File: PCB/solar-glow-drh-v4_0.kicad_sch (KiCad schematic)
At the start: 66 parts, among them J1 UPDI hdr, Q2 BSS138LT1G, SW2 LED master, U1 AVR64EA28 (VQFN28), U3 ADXL367, U5 NT3H2211, U6 TPS22917, U7 MB85RC512TY, U8 AEM10300, U9 TPS7A0233 (SOT23-5*)

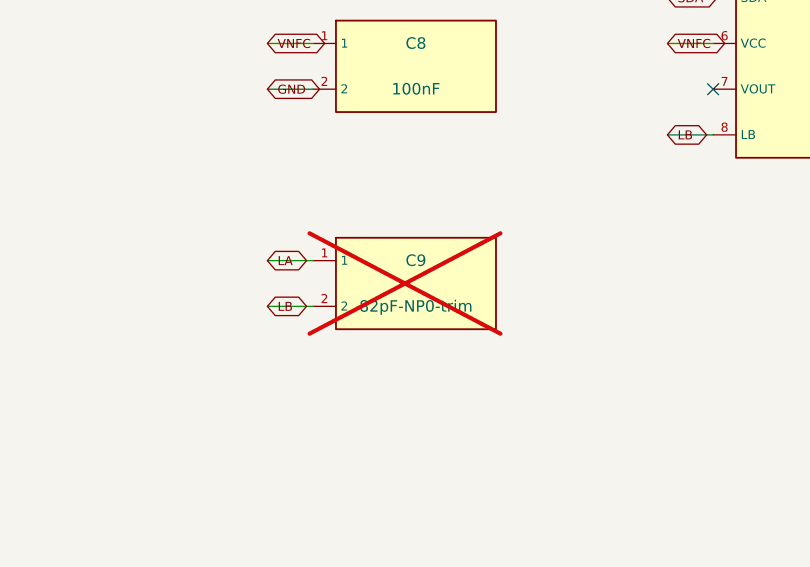
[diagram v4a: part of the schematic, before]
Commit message: C9: 82 pF DNP -> 47 pF placed, from a derivation rather than a bench trim
C9 was a hand-fitted trim. It is now a reflowed 47 pF part, because the value
can be computed and the computation lands well inside the window the trim would
have searched.

THE COIL. No closed form fits it: Wheeler, Mohan and Jenei are all fitted to
square spirals and this coil is 11.0 x 24.6 mm outer, aspect 2.2. So it is
Greenhouse on the board's own rails -- 7 turns read straight out of the .kicad_pcb
at x 37.4-41.0 / 44.8-48.4 and y 32.2-35.8 / 53.2-56.8, 0.30 mm trace on 0.60 mm
pitch -- summing the self-inductance of all 28 segments and the signed mutual
inductance of every parallel pair, GMD-corrected for strip width, 45-degree
corners taken off first order.

    L = 0.958 uH bare.  404 nH self + 606 nH mutual: 60% of this coil is coupling.

Checked twice. The same code agrees with Mohan's current-sheet fit to 2-6% on
square spirals, where that fit is valid. And PCB-side-notes §5's existing "~90 pF
bare" figure implies L = 0.957 uH at 13.56 MHz -- the same coil to three digits,
reached by whoever wrote that line without this calculation.

THE REST. Ci = 50 pF (NT3H2211 Table 42, LA-LB on-chip, 2.4 Vrms, 44/56 limits).
Cc = 6 pF (AN11276 Table 2: etched inter-turn 2-4, bridge 1-5 -- this coil's inner
end does return across the front on LB, which is that bridge).

THE TARGET IS NOT 13.56. AN11276 4.2.1: "For single tag operation, a tuning
slightly above 13.56 MHz would lead to maximum read-/write distance. Due to
manufacturing tolerances, a nominal frequency of 14.5 MHz for single tag operation
is recommended." Presenting the card couples the antennas and pulls the tag DOWN,
so a tag under the carrier gets worse as it approaches and one above it improves.

THE FERRITE IS A SCENARIO, NOT A TOLERANCE. §5's old 52-77 pF enclosed window is
an inductance window in disguise: +10% to +36%. Every board shares whichever
multiplier is real, so it is spanned, not stacked in quadrature with the comp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
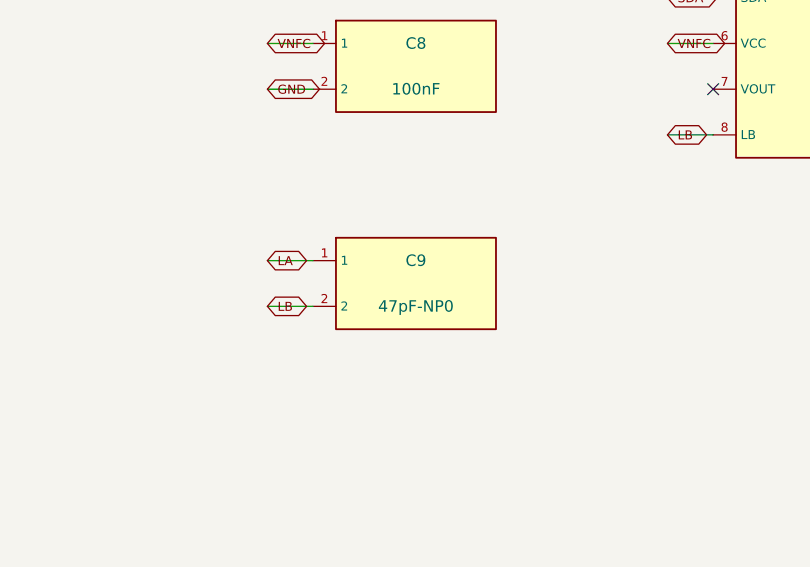
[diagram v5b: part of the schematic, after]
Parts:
- C9: value 82pF-NP0-trim -> 47pF-NP0; MPN QSCT251Q820G1GV001E -> QSCT251Q470G1GV001E; Supplier P/N 712-QSCT251Q820G1GV001ETR-ND -> 712-QSCT251Q470G1GV001ETR-ND; now fitted
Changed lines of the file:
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@@
 		(on_board yes)
 		(in_pos_files yes)
-		(dnp yes)
+		(dnp no)
 		(property "Reference" "C9"
 			(at 571.5 119.38 0)
@@
 			)
 		)
-		(property "Value" "82pF-NP0-trim"
+		(property "Value" "47pF-NP0"
 			(at 571.5 124.46 0)
 			(show_name no)
@@
 			)
 		)
-		(property "Description" "NFC tank trim, 0805 high-Q C0G +/-2% (Johanson S-series). DNP at assembly - hand-fit on the bench to land resonance at 13.56 MHz; U5 carries ~50 pF internally. Value is a STARTING POINT, trim 68-100 pF."
+		(property "Description" "NFC tank trim, 0805 high-Q C0G +/-2% (Johanson S-series, ultra-low ESR). PLACED at assembly as of 2026-07-30 - value derived, not trimmed: coil L = 0.958 uH by Greenhouse on the board's 7 rails, ferrite-loaded 1.05-1.30 uH, tag Ci = 50 pF (NT3H2211 Table 42), antenna Cc = 6 pF (AN11276 Table 2). 47 pF lands the enclosed resonance at 14.45 MHz against AN11276 4.2.1's 14.5 MHz single-tag target and stays above the 13.56 carrier across the whole ferrite range. Was 82 pF + DNP, which sat at 12.5 MHz enclosed - under the carrier, the wrong side to miss on."
 			(at 560.07 119.38 0)
 			(hide yes)
@@
 			)
 		)
-		(property "MPN" "QSCT251Q820G1GV001E"
+		(property "MPN" "QSCT251Q470G1GV001E"
 			(at 560.07 119.38 0)
 			(hide yes)
@@
 			)
 		)
-		(property "Supplier P/N" "712-QSCT251Q820G1GV001ETR-ND"
+		(property "Supplier P/N" "712-QSCT251Q470G1GV001ETR-ND"
 			(at 560.07 119.38 0)
 			(hide yes)

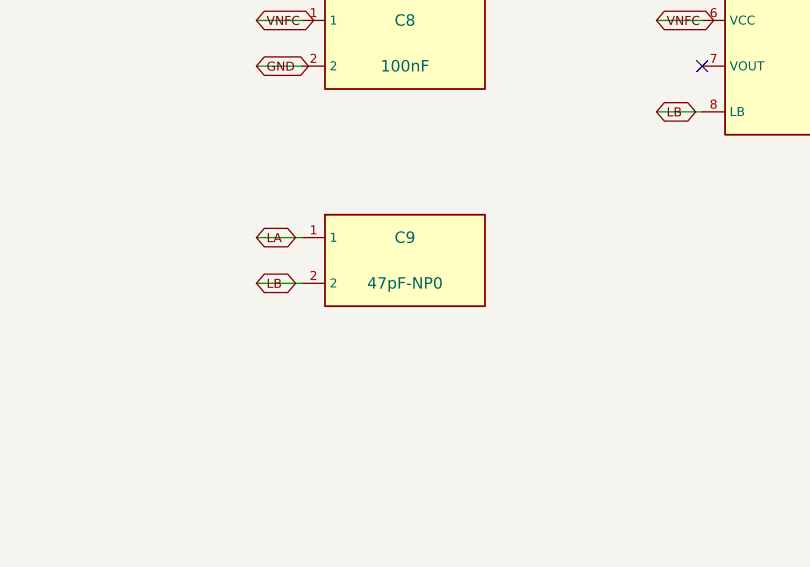
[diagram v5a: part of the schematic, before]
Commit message: Second full passive audit: two re-picks needed, one corner-case, C9 value fix
All 35 passives, audited holistically: schematic + board + BOM cross-check,
per-pad nets, node worst-case voltages, DC-bias derating, datasheet-required
values for every IC's externals, and a live two-distributor sourcing sweep.

FINDING 1 (the real one). C25, the AEM10300's CSRC/BUFSRC buffer, is
GRT188R61A226ME13D -- 0603, 22 uF, X5R, 10 V. The AEM's table says CSRC min 13 /
typ 22 uF, and its footnote says verbatim: "Consider all component tolerance and
deratings. Typically, DC-bias derating has a major impact on capacitance on
ceramic capacitors." BUFSRC rides the MPP at 3.1-3.5 V and touches VOC 4.15 V; a
0603 22 uF/10 V X5R loses 45-60% there, leaving ~9-12 uF -- under the minimum
the footnote exists to warn about. Fix verified in stock and verified to FIT:
TDK C2012X5R1C226M125AC (0805, 16 V, 1.25 mm, 11,799 at DK) gives ~15-17 uF
effective; measured neighbour gaps at C25 (SC3 0.529 / L2 0.575 / SB2 0.776 mm)
leave >=0.28 mm after 0603->0805 growth. A 1206 does not fit (L2 would be at
0.02 mm). part_heights "C25": 0.90 -> 1.25 with the swap.

FINDING 2. C26/C27's GRM21BR71A106KA73L (0805 10 uF X7R 10 V): zero stock at
DigiKey in all three package types AND no availability at Mouser; the automotive
sibling is NRND. Live candidate: Samsung CL21B106KOQNNNG, 16 V X7R, 4,292 at
Mouser -- which also halves C27's derating (it sits on STO at 5.5 V, 55% of a
10 V rating, ~-40%). The catch is recorded with it: the Samsung part is 1.40 mm
tall, so part_heights C26/C27 must go 1.25 -> 1.45 in the same commit or the
brace pockets are cut 0.15 mm short -- the exact silent failure that file's
docstring documents.

FINDING 3 (corner case, no copper change). R1-R4 are 1/16 W 0402s; at the worst
corner (STO 5.5 V, min-bin Vf 1.9, VOL 0.4, 100% duty) they dissipate ~68-70 mW
= ~110% of rating. Typical is ~22 mW and PWM keeps averages far lower. Cheapest
guard is a duty clamp above STO ~5.2 V in the pr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
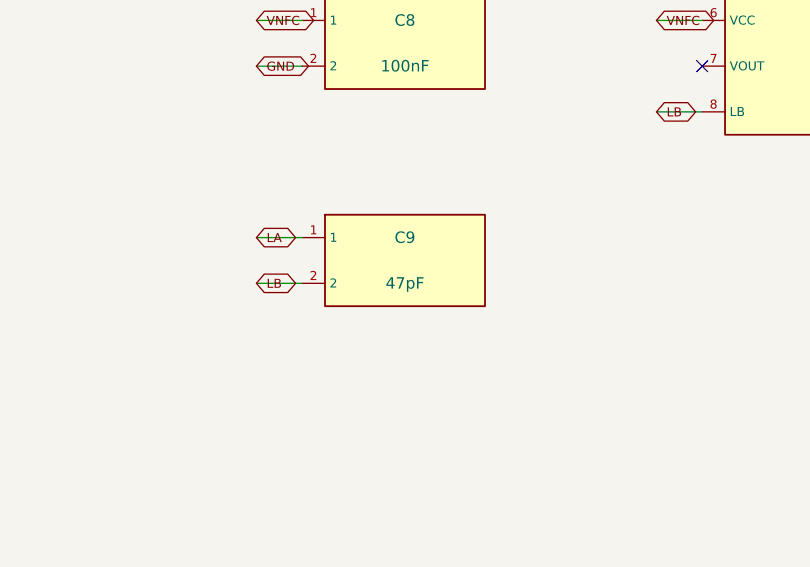
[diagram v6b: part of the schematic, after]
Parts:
- C9: value 47pF-NP0 -> 47pF
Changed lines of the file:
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@@
 			)
 		)
-		(property "Value" "47pF-NP0"
+		(property "Value" "47pF"
 			(at 571.5 124.46 0)
 			(show_name no)

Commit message: Land both audit re-picks: C26/C27 complete, C25 complete except its land (tripwire armed)
The two capacitor re-picks from passive audit #2, as one change set.

C26/C27 -> Samsung CL21B106KOQNNNG (10 uF, 0805, X7R, 16 V). Complete in this
commit: schematic, board metadata, both BOM files, and part_heights 1.25 -> 1.45
(the Samsung body is 1.40 max; against the generic 1.25 model that is a 0.20
overshoot, inside OVERSHOOT_MAX -- deliberate air, pocket deepens, safe
direction). Same 0805 land, so nothing else moves. Why: the old
GRM21BR71A106KA73L is stock-zero at DigiKey in all three package types and
unavailable at Mouser, with the automotive sibling NRND; 16 V also halves the
DC-bias loss on C27's 5.5 V STO node (was at 55% of a 10 V rating). Mouser
187-CL21B106KOQNNNG, 4,292 in stock, $0.22 q1, verified live today. Supplier
fields flipped DigiKey -> Mouser accordingly.

C25 -> TDK C2012X5R1C226M125AC (22 uF, 0805, X5R, 16 V). Everything EXCEPT the
land lands here: schematic (footprint -> C_0805_2012Metric + MPN + DK
445-7647-1-ND, 11,799 in stock, $0.56 q1), board metadata, both BOM files. The
BOARD still carries the 0603 land, so this commit is DELIBERATELY RED twice
over, by the same tripwire pattern C9 used: DRC footprint_symbol_mismatch
(error) and consistency check [1]'s footprint comparison (error) both name
exactly C25 and nothing else. To clear: Update PCB from Schematic (C25 keeps
its centroid at (25.15, 55.0) r90; pad 1 = BUFSRC, pad 2 = GND), and flip
part_heights "C25": 0.90 -> 1.25 IN THE SAME COMMIT -- it stays 0.90 here on
purpose, because check [7] measures the declared height against the model on
the board, and 1.25 against the still-0603 body is a 0.45 overshoot that check
[7] would rightly reject; the file's comment carries this reasoning. Why the
re-pick: the 0603/10 V part holds ~9-12 uF at the 3.1-4.15 V BUFSRC bias
against the AEM10300's 13 uF effective minimum, whose own footnote names
DC-bias derating; the 16 V 0805 holds ~15-17 uF, fits in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
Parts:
- C25: footprint Capacitor_SMD:C_0603_1608Metric -> Capacitor_SMD:C_0805_2012Metric; MPN GRT188R61A226ME13D -> C2012X5R1C226M125AC; Supplier P/N 490-GRT188R61A226ME13DCT-ND -> 445-7647-1-ND
- C26, C27: MPN GRM21BR71A106KA73L -> CL21B106KOQNNNG; Supplier DigiKey -> Mouser; Supplier P/N 490-10516-1-ND -> 187-CL21B106KOQNNNG (Mouser)
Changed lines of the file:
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@@
 			)
 		)
-		(property "Footprint" "Capacitor_SMD:C_0603_1608Metric"
+		(property "Footprint" "Capacitor_SMD:C_0805_2012Metric"
 			(at 592.66 387.35 0)
 			(show_name no)
@@
 			)
 		)
-		(property "Description" "22uF 10V 0603 X5R, AEM SRC decoupling (aem10300.pdf Table 11 CSRC)"
+		(property "Description" "22uF 16V 0805 X5R, AEM CSRC buffer at BUFSRC (aem10300 Table 6: min 13uF EFFECTIVE - footnote 1 names DC-bias derating). Re-picked 2026-07-30 (audit #2) from 0603/10V GRT188R61A226ME13D, which held only ~9-12uF at the 3.1-4.15V MPP bias. 16V 0805 holds ~15-17uF. 1.25mm max. Fits in place (gaps SC3 0.529/L2 0.575/SB2 0.776mm); 1206 does NOT fit."
 			(at 581.66 372.11 0)
 			(show_name no)
@@
 			)
 		)
-		(property "MPN" "GRT188R61A226ME13D"
+		(property "MPN" "C2012X5R1C226M125AC"
 			(at 581.66 372.11 0)
 			(show_name no)
@@
 			)
 		)
-		(property "Supplier P/N" "490-GRT188R61A226ME13DCT-ND"
+		(property "Supplier P/N" "445-7647-1-ND"
 			(at 459.74 372.11 0)
 			(hide yes)
@@
 			)
 		)
-		(property "Description" "10uF 10V 0805 X7R, AEM VINT buffer"
+		(property "Description" "10uF 16V 0805 X7R, AEM VINT buffer. Re-picked 2026-07-30 (audit #2): GRM21BR71A106KA73L went stock-zero at DigiKey AND Mouser, auto sibling NRND. 16V also margins the family. 1.40mm max -> part_heights C26/C27 = 1.45."
 			(at 612.14 372.11 0)
 			(show_name no)
@@
 			)
 		)
-		(property "MPN" "GRM21BR71A106KA73L"
+		(property "MPN" "CL21B106KOQNNNG"
 			(at 612.14 372.11 0)
 			(show_name no)
@@
 			)
 		)
-		(property "Supplier" "DigiKey"
-			(at 459.74 372.11 0)
-			(hide yes)
-			(show_name no)
-			(do_not_autoplace no)
-			(effects
-				(font
-					(size 1.27 1.27)
-				)
-			)
-		)
-		(property "Supplier P/N" "490-10516-1-ND"
+		(property "Supplier" "Mouser"
+			(at 459.74 372.11 0)
+			(hide yes)
+			(show_name no)
+			(do_not_autoplace no)
+			(effects
+				(font
+					(size 1.27 1.27)
+				)
+			)
+		)
+		(property "Supplier P/N" "187-CL21B106KOQNNNG (Mouser)"
 			(at 459.74 372.11 0)
 			(hide yes)
@@
 			)
 		)
-		(property "Description" "10uF 10V 0805 X7R, STO local bulk/decoupling"
+		(property "Description" "10uF 16V 0805 X7R, STO local bulk/decoupling. Re-picked 2026-07-30 (audit #2): GRM21BR71A106KA73L went stock-zero at DigiKey AND Mouser, auto sibling NRND. 16V halves the DC-bias loss at STO's 5.5V max (was 55% of a 10V rating). 1.40mm max -> part_heights 1.45."
 			(at 642.62 372.11 0)
 			(show_name no)
@@
 			)
 		)
-		(property "MPN" "GRM21BR71A106KA73L"
+		(property "MPN" "CL21B106KOQNNNG"
 			(at 642.62 372.11 0)
 			(show_name no)
@@
 			)
 		)
-		(property "Supplier" "DigiKey"
-			(at 459.74 372.11 0)
-			(hide yes)
-			(show_name no)
-			(do_not_autoplace no)
-			(effects
-				(font
-					(size 1.27 1.27)
-				)
-			)
-		)
-		(property "Supplier P/N" "490-10516-1-ND"
-			(at 459.74 372.11 0)
-			(hide yes)
+		(property "Supplier" "Mouser"
+			(at 459.74 372.11 0)
+			(hide yes)
+			(show_name no)
+			(do_not_autoplace no)
+			(effects
+				(font
+					(size 1.27 1.27)
+				)
+			)
+		)
+		(property "Supplier P/N" "187-CL21B106KOQNNNG (Mouser)"
+			(at 459.74 372.11 0)
+			(hide yes)

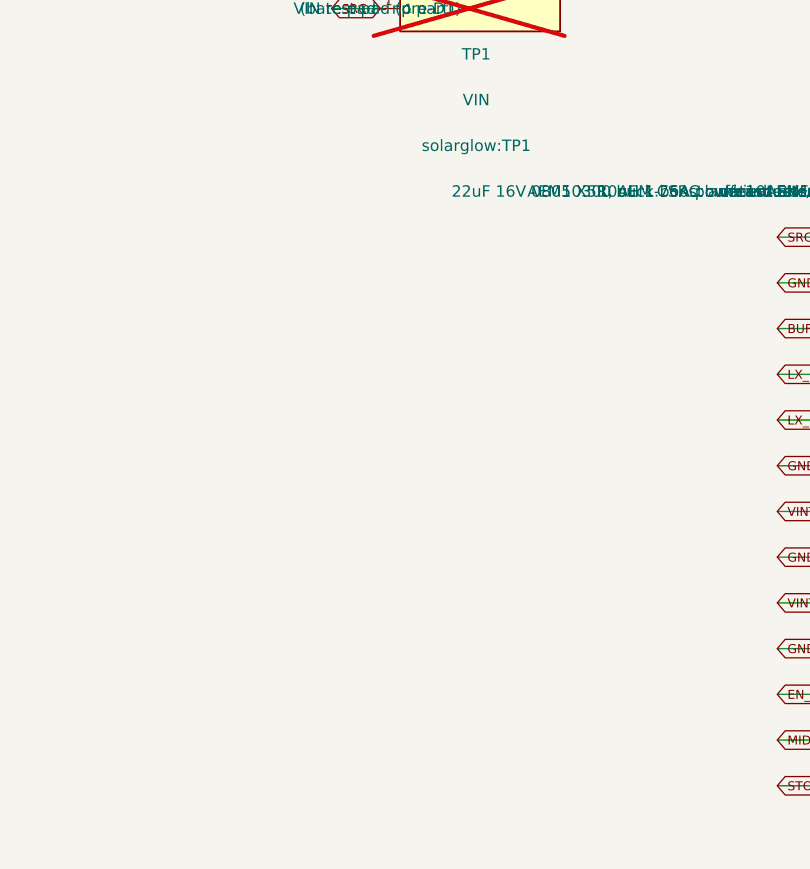
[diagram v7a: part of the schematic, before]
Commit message: Test pads TP2-TP7 on the harvest chain + panel tooling holes TH1/TH2
The whole harvester subsystem was unprobeable (audit find): only GND, SRC,
STO, SCL, SDA, UPDI had probe access. Six new 1.0 mm bare pads on B.Cu fix
that, in bring-up order: TP2 VS (5.07, 14.32) and TP3 MID (25.4, 11.1)
directly on their tracks in the open; TP4 LX_LOUT (28.45, 57.45) stub-fed
0.49 mm (switch node - shortest stub on purpose); TP5 VINT (32.25, 50.42);
TP6 BUFSRC (29.9, 57.55) via a 10.5 mm channel route south of L2; TP7
STO_LDO (3.5, 63.9) down the left edge channel at 0.55 mm from the outline
(the board's 0.5 mm floor, not the 0.381 DRU gate, is what governs there).
Sites are exhaustively scanned: on own-net copper, >=0.152 to ALL other
copper including the other five target nets (the first BUFSRC route missed
that class of obstacle and DRC caught it on a VINT track - re-solved),
outside courtyards so a pogo can land, >=0.30 from drills, off rule areas.
Schematic mirrors the TP1/SRC pattern: solarglow:TP1 instances, footprint
solarglow:TPB (embedded like TP1), 5.08 mm wires to input global labels.

panelize.py grows the matching fixture registration: two 1.5 mm NPTH in
the side rails at y=20 (left) / y=85 (right), 16.1 mm off 180-degree
symmetry so a backwards panel refuses the pins - asserted in main(). The
plating-bus ring runs exactly where the holes want to be, so it jogs
outward 1.55 around each: 0.300 hole-to-ring, 0.45 copper-to-edge,
verified on the emitted panel (ring stays one piece, touches both spurs).

Guards: DRC 0 live errors (excluded set unchanged: 10 errors + 3 silk),
parity 0, unconnected 0, mask-bridge 202 (noise band 200-223), zero
F.Mask hits; ERC 3 excluded baseline warnings; mask_art MATCH;
part_colors MATCH; consistency 0/0. Stored GND fills overlap the new
copper until the next KiCad save refills (CI DRC refills before checking).
BOMs: master TP row widened to TP1-TP7, assembly "Not placed" updated.
Both TODO blocks culled; full derivation in the design-no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
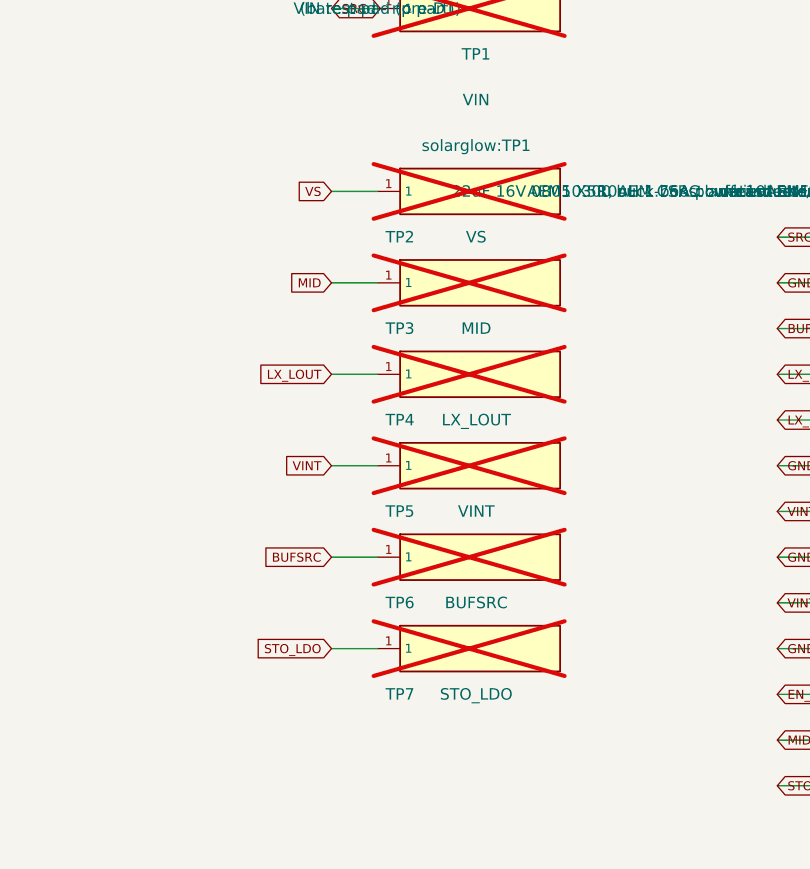
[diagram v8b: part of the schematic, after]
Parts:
- added TP2: VS, solarglow:TPB, symbol solarglow:TP1
- added TP3: MID, solarglow:TPB, symbol solarglow:TP1
- added TP4: LX_LOUT, solarglow:TPB, symbol solarglow:TP1
- added TP5: VINT, solarglow:TPB, symbol solarglow:TP1
- added TP6: BUFSRC, solarglow:TPB, symbol solarglow:TP1
- added TP7: STO_LDO, solarglow:TPB, symbol solarglow:TP1
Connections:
- net BUFSRC: now also TP6.1
- net LX_LOUT: now also TP4.1
- net MID: now also TP3.1
- net STO_LDO: now also TP7.1
- net VINT: now also TP5.1
- net VS: now also TP2.1
